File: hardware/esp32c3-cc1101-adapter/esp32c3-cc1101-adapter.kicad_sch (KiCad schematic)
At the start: 3 parts, among them J1 Conn_01x08, J2 Conn_01x08, J3 E07-M1101D

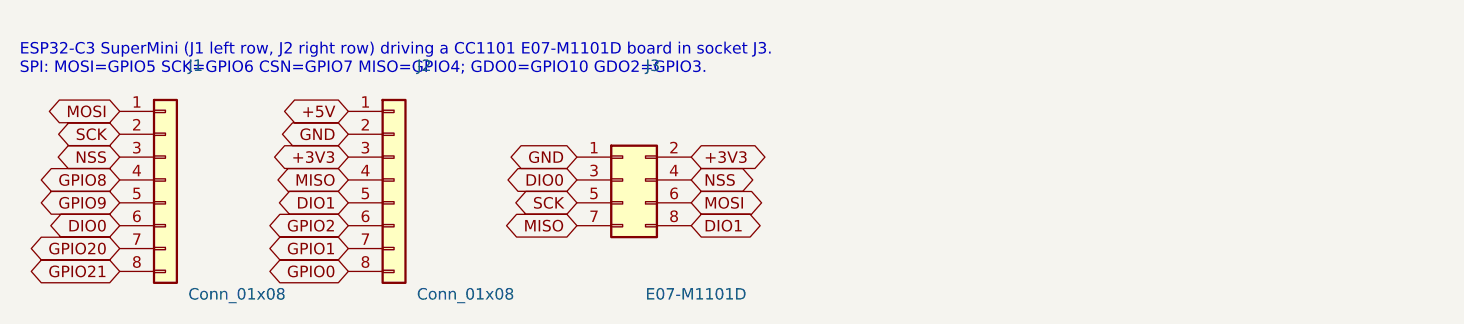
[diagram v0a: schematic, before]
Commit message: Make the CC1101 adapter single-sided; add ESP32 pin names to silk
All tracks of the ESP32-C3 to CC1101 adapter now run on B.Cu (the
front keeps only the through-hole pad rings).  To make the eight nets
planar without jumpers the SuperMini lies on its side with USB-C off
the left edge, so its GPIO row sits above the socket and its power row
behind it; MISO and GDO2 go over the top of the power row and down the
left edge.  Board is 30 x 38 mm.

Both adapters now print the SuperMini's own pin names on the outer
side of each header row and the radio signal names on the inner side.
Layout plots now include B.Cu.

Co-Authored-By: Claude Fable 5.1 <noreply@anthropic.com>
Claude-Session: https://claude.ai/code/session_01JoGdh4Cg3VtTTDZi4gQuiN
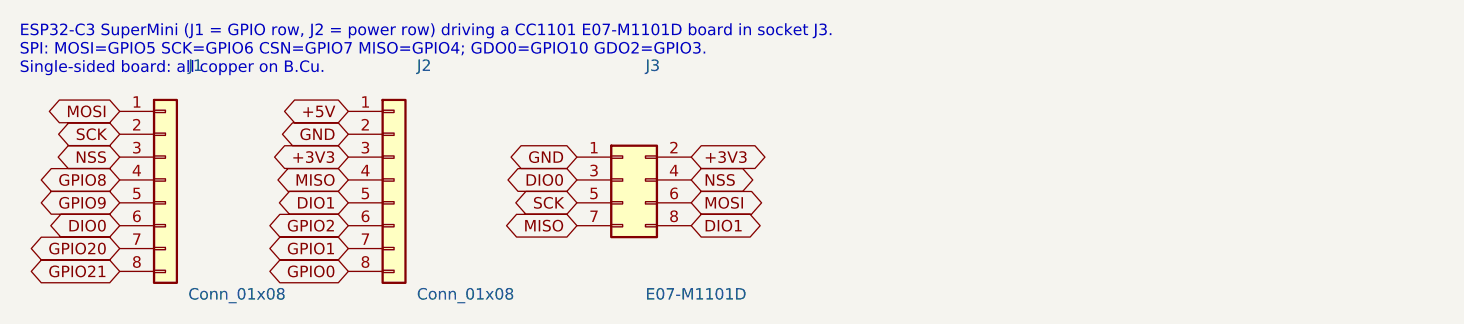
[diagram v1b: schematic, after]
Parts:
- J1, J2: footprint Adapter:SuperMini_Header_1x08_P2.54mm_THT -> Adapter:SuperMini_Header_1x08_P2.54mm_THT_Row
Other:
- note added: "ESP32-C3 SuperMini (J1 = GPIO row, J2 = power row) driving a CC1101 E07-M1101D board in socket J3. SPI: MOSI=GPIO5 SCK=GPIO6 CSN=GPIO7 MISO=GPIO4; GDO0=GPIO10 GDO2=GPIO3. Single-sided board: all copper on B.Cu."
- note removed: "ESP32-C3 SuperMini (J1 left row, J2 right row) driving a CC1101 E07-M1101D board in socket J3. SPI: MOSI=GPIO5 SCK=GPIO6 CSN=GPIO7 MISO=GPIO4; GDO0=GPIO10 GDO2=GPIO3."
- title: ESP32-C3 SuperMini to CC1101 E07-M1101D adapter -> ESP32-C3 SuperMini to CC1101 E07-M1101D adapter (single-sided)
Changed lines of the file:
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@@
 	(paper "A4")
 	(title_block
-		(title "ESP32-C3 SuperMini to CC1101 E07-M1101D adapter")
+		(title "ESP32-C3 SuperMini to CC1101 E07-M1101D adapter (single-sided)")
 		(rev "1")
-		(comment 1 "Carrier joining an ESP32-C3 SuperMini to an Ebyte E07-M1101D-SMA CC1101 433MHz board via a 2x4 socket")
+		(comment 1 "Single-sided carrier joining an ESP32-C3 SuperMini to an Ebyte E07-M1101D-SMA CC1101 433MHz board via a 2x4 socket")
 	)
 	(symbol
@@
 			)
 		)
-		(property "Footprint" "Adapter:SuperMini_Header_1x08_P2.54mm_THT"
+		(property "Footprint" "Adapter:SuperMini_Header_1x08_P2.54mm_THT_Row"
 			(at 76.2 101.6 0)
 			(effects
@@
 			)
 		)
-		(property "Description" "ESP32-C3 SuperMini left row"
+		(property "Description" "ESP32-C3 SuperMini GPIO row (left column)"
 			(at 76.2 101.6 0)
 			(effects
@@
 			)
 		)
-		(property "Footprint" "Adapter:SuperMini_Header_1x08_P2.54mm_THT"
+		(property "Footprint" "Adapter:SuperMini_Header_1x08_P2.54mm_THT_Row"
 			(at 101.6 101.6 0)
 			(effects
@@
 			)
 		)
-		(property "Description" "ESP32-C3 SuperMini right row"
+		(property "Description" "ESP32-C3 SuperMini power row (right column)"
 			(at 101.6 101.6 0)
 			(effects
@@
 		)
 	)
-	(text "ESP32-C3 SuperMini (J1 left row, J2 right row) driving a CC1101 E07-M1101D board in socket J3.\nSPI: MOSI=GPIO5 SCK=GPIO6 CSN=GPIO7 MISO=GPIO4; GDO0=GPIO10 GDO2=GPIO3."
+	(text "ESP32-C3 SuperMini (J1 = GPIO row, J2 = power row) driving a CC1101 E07-M1101D board in socket J3.\nSPI: MOSI=GPIO5 SCK=GPIO6 CSN=GPIO7 MISO=GPIO4; GDO0=GPIO10 GDO2=GPIO3.\nSingle-sided board: all copper on B.Cu."
 		(exclude_from_sim no)
 		(at 60 90 0)

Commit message: Rework the CC1101 adapter: castellated keyhole pads, corner holes, two-sided silk
* SuperMini pins land on keyhole pads (1.0 mm hole plus 1.6 x 3.4 mm oval
  copper reaching 1.2 mm past the SuperMini edge) so the module can be
  fitted with header pins or soldered flat by its castellations.
* The SuperMini body now overhangs the left edge by 0.5 mm so the USB-C
  connector hangs clear of the board.
* Four M2 mounting holes 2.4 mm in from the corners; the socket moves right
  so the plugged-in E07 board clears the bottom-left screw.
* Silkscreen on both sides (back copy mirrored), signal names next to the
  SuperMini use the CC1101's names (GDO0, GDO2, CSN).
* Board is 27 x 36.5 mm; all tracks stay on B.Cu.  MISO and GDO2 now run
  over the top of the power row, down the right of the SuperMini and under
  the socket.
* kicadgen: gr_line helper.

Co-Authored-By: Claude Fable 5.1 <noreply@anthropic.com>
Claude-Session: https://claude.ai/code/session_01JoGdh4Cg3VtTTDZi4gQuiN
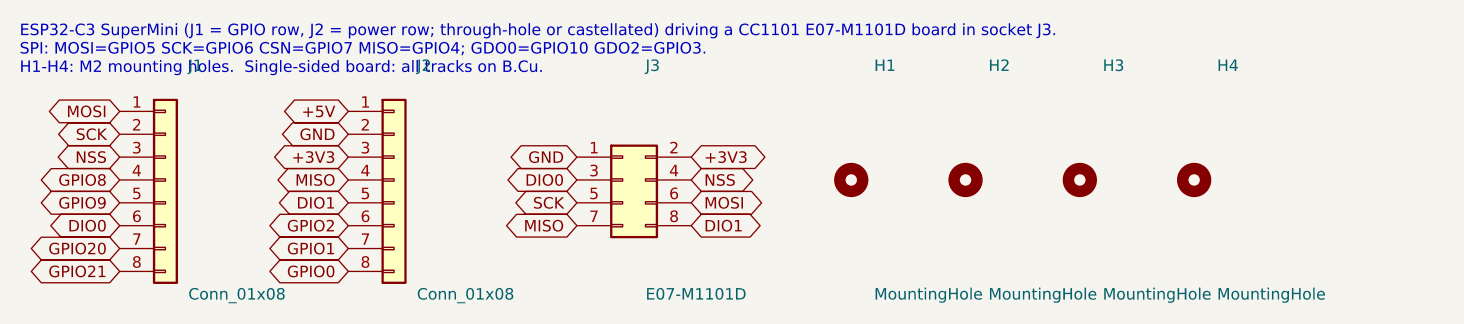
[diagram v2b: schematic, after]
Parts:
- added H1, H2, H3, H4: MountingHole, Adapter:MountingHole_2.2mm_M2, symbol Mechanical:MountingHole
- J1: footprint Adapter:SuperMini_Header_1x08_P2.54mm_THT_Row -> Adapter:SuperMini_Row_1x08_P2.54mm_THT_Castellated_Down
- J2: footprint Adapter:SuperMini_Header_1x08_P2.54mm_THT_Row -> Adapter:SuperMini_Row_1x08_P2.54mm_THT_Castellated_Up
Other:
- note added: "ESP32-C3 SuperMini (J1 = GPIO row, J2 = power row; through-hole or castellated) driving a CC1101 E07-M1101D board in socket J3. SPI: MOSI=GPIO5 SCK=GPIO6 CSN=GPIO7 MISO=GPIO4; GDO0=GPIO10 GDO2=GPIO3. H1-H4: M2 mounting holes. Single-sided board: all tracks on B.Cu."
- note removed: "ESP32-C3 SuperMini (J1 = GPIO row, J2 = power row) driving a CC1101 E07-M1101D board in socket J3. SPI: MOSI=GPIO5 SCK=GPIO6 CSN=GPIO7 MISO=GPIO4; GDO0=GPIO10 GDO2=GPIO3. Single-sided board: all copper on B.Cu."

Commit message: CC1101 adapter GND pour with antenna keepout; optional SMA on the SX1278 adapter
* kicadgen: Zone (copper pour / keepout) support, board revision "0" in
  every title block, KICAD_SHARE overridable for non-snap installs.
* scripts/fill_zones.py: fills zones with KiCad's own filler (pcbnew python,
  re-executed inside the snap when needed) and splices only the fill
  polygons into the generated file, so generation stays reproducible.
* CC1101 adapter: GND pour on F.Cu (all tracks remain on B.Cu), keepout on
  both layers under the SuperMini's ceramic antenna; MISO/GDO2 now run
  outside the SuperMini body instead of under its antenna.
* SX1278 adapter: 24 x 58 mm, optional edge-mount SMA jack (J4) on the
  bottom edge fed from the wire-hole antenna trace, ground legs on B.Cu
  with vias to the front pads.

Co-Authored-By: Claude Fable 5.1 <noreply@anthropic.com>
Claude-Session: https://claude.ai/code/session_01JoGdh4Cg3VtTTDZi4gQuiN
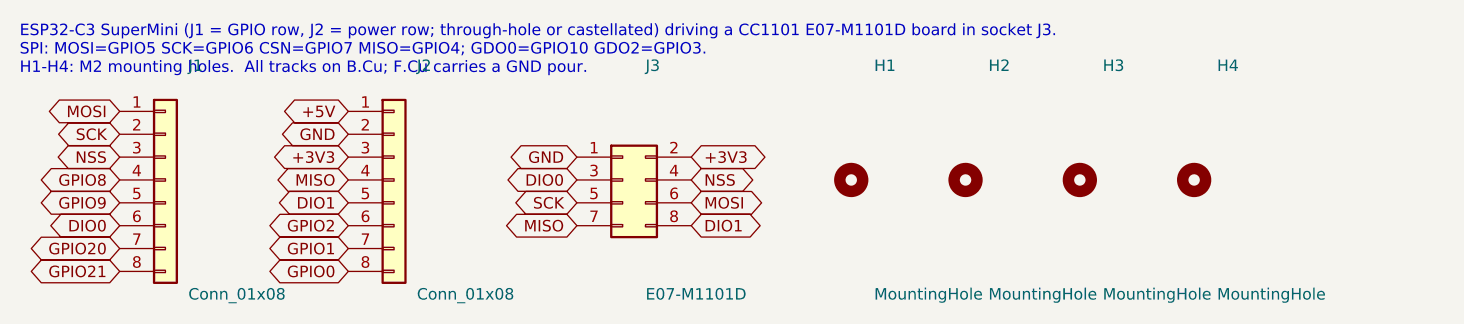
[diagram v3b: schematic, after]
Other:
- note added: "ESP32-C3 SuperMini (J1 = GPIO row, J2 = power row; through-hole or castellated) driving a CC1101 E07-M1101D board in socket J3. SPI: MOSI=GPIO5 SCK=GPIO6 CSN=GPIO7 MISO=GPIO4; GDO0=GPIO10 GDO2=GPIO3. H1-H4: M2 mounting holes. All tracks on B.Cu; F.Cu carries a GND pour."
- note removed: "ESP32-C3 SuperMini (J1 = GPIO row, J2 = power row; through-hole or castellated) driving a CC1101 E07-M1101D board in socket J3. SPI: MOSI=GPIO5 SCK=GPIO6 CSN=GPIO7 MISO=GPIO4; GDO0=GPIO10 GDO2=GPIO3. H1-H4: M2 mounting holes. Single-sided board: all tracks on B.Cu."
- title: ESP32-C3 SuperMini to CC1101 E07-M1101D adapter (single-sided) -> ESP32-C3 SuperMini to CC1101 E07-M1101D adapter
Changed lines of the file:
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@@
 	(paper "A4")
 	(title_block
-		(title "ESP32-C3 SuperMini to CC1101 E07-M1101D adapter (single-sided)")
-		(rev "1")
-		(comment 1 "Single-sided carrier joining an ESP32-C3 SuperMini to an Ebyte E07-M1101D-SMA CC1101 433MHz board via a 2x4 socket")
+		(title "ESP32-C3 SuperMini to CC1101 E07-M1101D adapter")
+		(rev "0")
+		(comment 1 "Carrier joining an ESP32-C3 SuperMini to an Ebyte E07-M1101D-SMA CC1101 433MHz board via a 2x4 socket; all tracks on the back, GND pour on the front")
 	)
 	(symbol
@@
 		)
 	)
-	(text "ESP32-C3 SuperMini (J1 = GPIO row, J2 = power row; through-hole or castellated) driving a CC1101 E07-M1101D board in socket J3.\nSPI: MOSI=GPIO5 SCK=GPIO6 CSN=GPIO7 MISO=GPIO4; GDO0=GPIO10 GDO2=GPIO3.\nH1-H4: M2 mounting holes.  Single-sided board: all tracks on B.Cu."
+	(text "ESP32-C3 SuperMini (J1 = GPIO row, J2 = power row; through-hole or castellated) driving a CC1101 E07-M1101D board in socket J3.\nSPI: MOSI=GPIO5 SCK=GPIO6 CSN=GPIO7 MISO=GPIO4; GDO0=GPIO10 GDO2=GPIO3.\nH1-H4: M2 mounting holes.  All tracks on B.Cu; F.Cu carries a GND pour."
 		(exclude_from_sim no)
 		(at 60 90 0)
